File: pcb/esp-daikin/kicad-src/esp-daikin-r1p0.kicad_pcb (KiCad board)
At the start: 2 copper layers, 28.6 x 30 mm, 38 parts, among them J1 PH_01x05, J2 PinHeader 1x02, U1 ESP32-C3-MINI-1, U3 AOZ1280CI

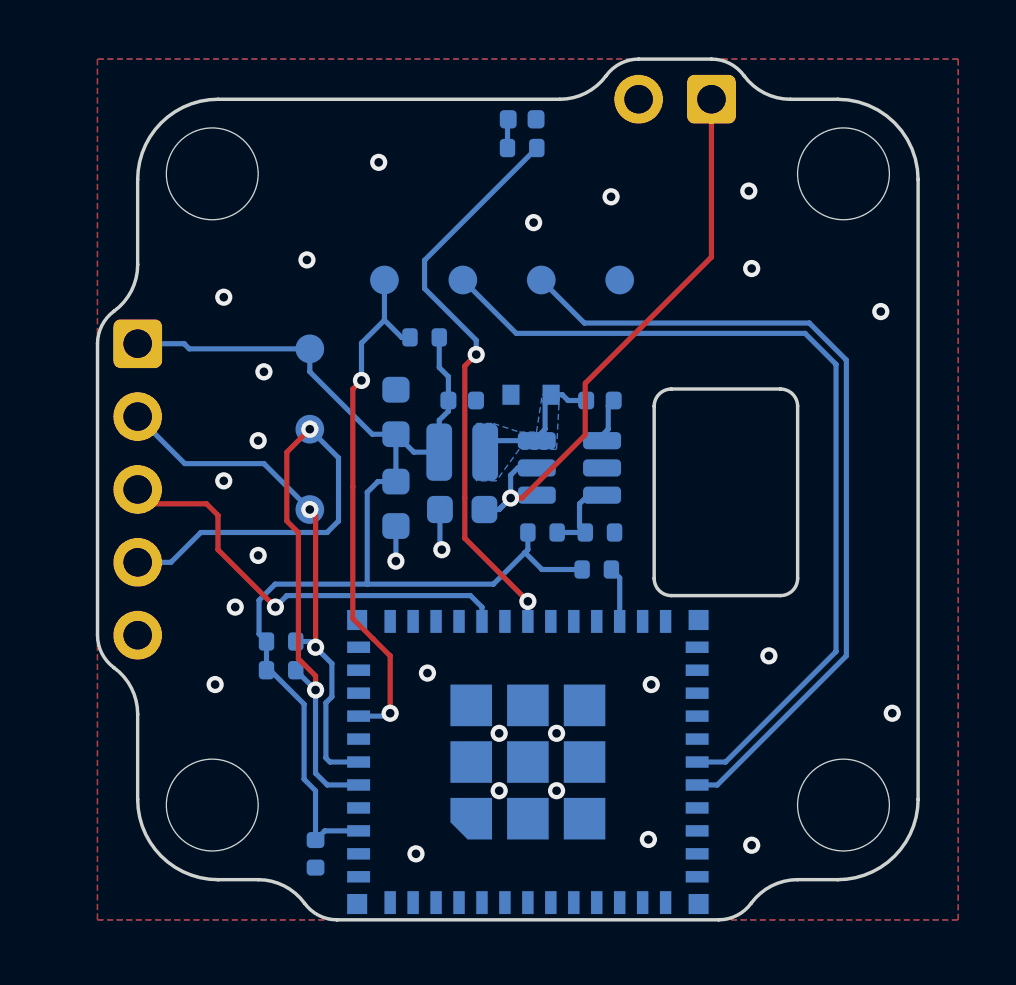
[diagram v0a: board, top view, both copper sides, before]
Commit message: pcb: Update daikin-esp
 - Add test-point for GPIO9
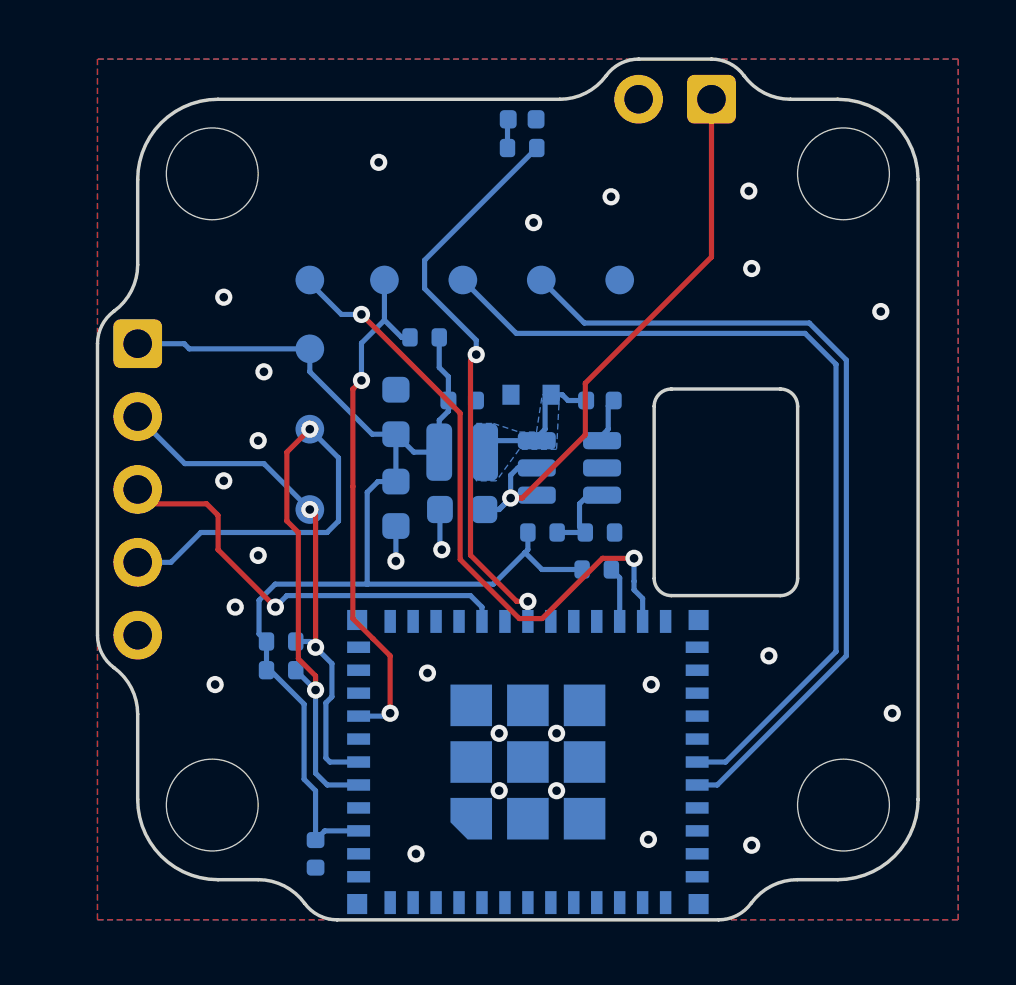
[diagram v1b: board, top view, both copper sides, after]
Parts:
- added TP4: JDB_CTRL, TestPoint:TestPoint_Pad_D1.0mm, B.Cu at (169.4, 80.2)
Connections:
- U1 pad 23: unconnected-(U1-GPIO9-Pad23) -> Net-(U1-GPIO9)
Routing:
- net Net-(U1-GPIO9): track 0.00 -> 22.4 mm, vias 0 -> 2
- net GND: vias 27 -> 26
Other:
- board text added: "boot"
- board text removed: "pu"

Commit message: pcb: Flip daikin-esp design
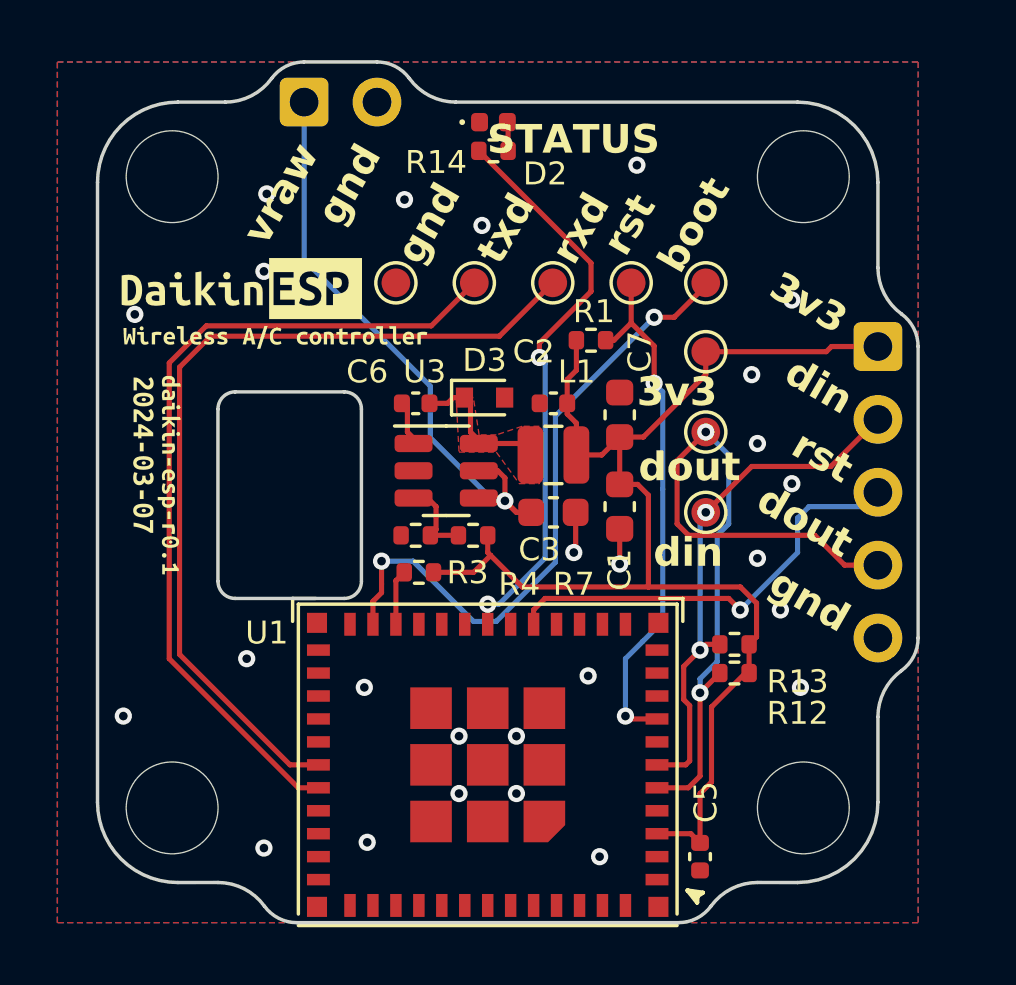
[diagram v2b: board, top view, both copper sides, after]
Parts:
- removed kibuzzard-65B62B21: G***, kibuzzard-65B62B21
- removed kibuzzard-65E1AE16: G***, kibuzzard-65E1AE16
- C1, C2, C3, C5, C6, C7, D2, D3, L1, R1, R12, R13, R14, R3, R4, R7, TP1, TP11, TP12, TP2, TP3, TP4, TP8, TP9, U1, U3, kibuzzard-65E1B005, kibuzzard-65E1B071, kibuzzard-65E1B080, kibuzzard-65E1B0DF, kibuzzard-65E9962C: moved to F.Cu
- H1, H2, H3, H4, J1, J2: moved to B.Cu
- moved J1 25.8 mm to (189.2, 82.5), turned to 180 degrees
- moved kibuzzard-65E9962C 25.4 mm to (163.6, 86.3)
- moved kibuzzard-65E1B005 23.6 mm to (164.5, 87.0)
- moved H1 23.4 mm to (164.6, 76.6), turned to 180 degrees
- moved H4 23.4 mm to (164.6, 98.6), turned to 180 degrees
- moved kibuzzard-65E1B071 22.0 mm to (165.3, 80.5), turned to 0 degrees
- moved H2 20.6 mm to (186.6, 76.6), turned to 180 degrees
- moved H3 20.6 mm to (186.6, 98.6), turned to 180 degrees
- moved kibuzzard-65E1B0DF 16.2 mm to (168.2, 82.2), turned to 0 degrees
- moved R12 15.8 mm to (184.2, 93.9), turned to 180 degrees
- moved R13 15.8 mm to (184.2, 92.9), turned to 180 degrees
- moved J2 14.2 mm to (169.2, 74.0)
- moved TP12 13.8 mm to (183.2, 82.7), turned to 0 degrees
- moved TP4 13.8 mm to (183.2, 80.3), turned to 0 degrees
- moved TP8 13.8 mm to (183.2, 85.5), turned to 0 degrees
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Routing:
- added copper zone on F.Cu, net Net-(D3-K)
- removed copper zone on B.Cu, net Net-(D3-K)
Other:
- outline, holes or cut-outs redrawn
- board text added: "vraw"
